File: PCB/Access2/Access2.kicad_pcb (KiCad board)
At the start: 2 copper layers, 50 x 26.5 mm, 67 parts, among them J1 USB-C, J2 RFID, J3 INPUTS, J4 Shelly, J5 POWER, J6 DOOR, Q1 NX7002AK, SW1 ESE13V01D, U1 ESP32-PICO-MINI-02, U2 FT231XQ, U3 G3VM-41GR8, U4 LMR16006XDDCR, U5 LMR16006XDDCR, U6 AA, U7 QR

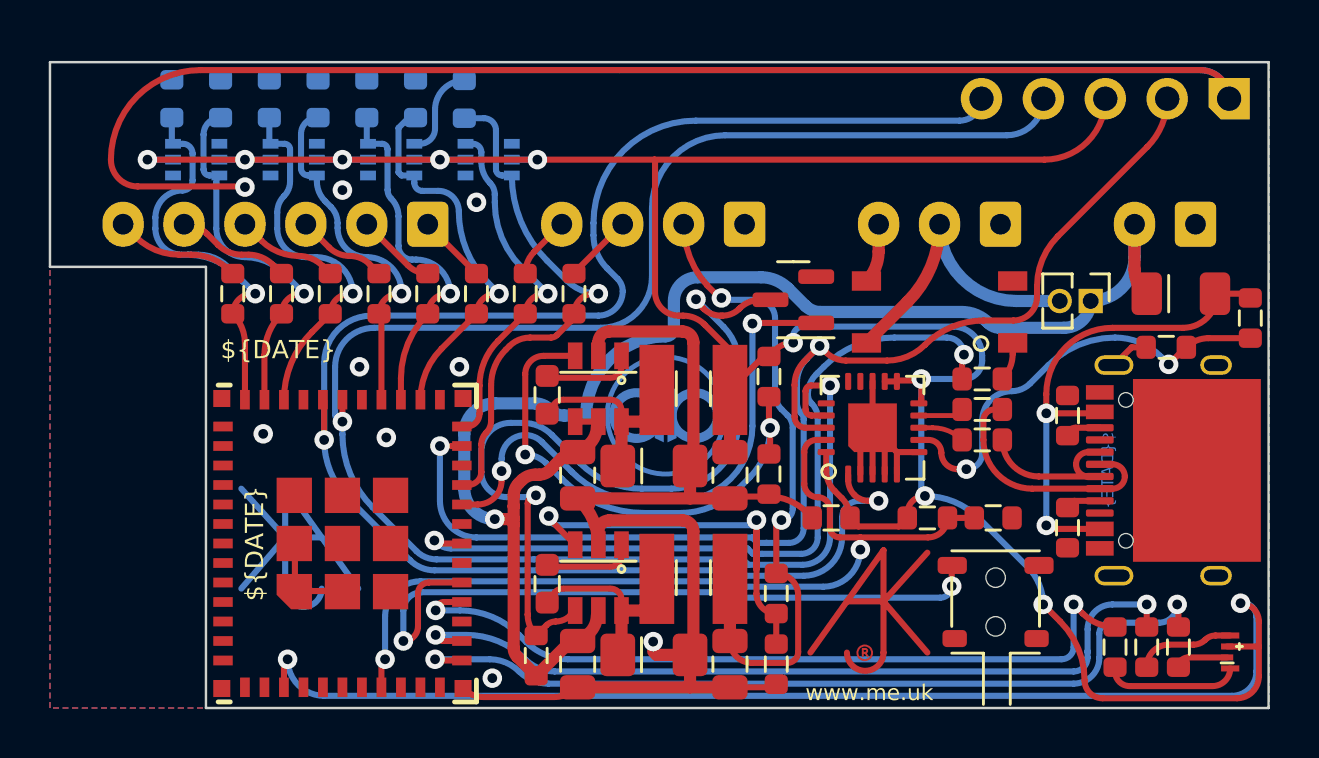
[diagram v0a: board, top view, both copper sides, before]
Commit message: Reverse polarity protection and additional capacitors for less clean supplies.
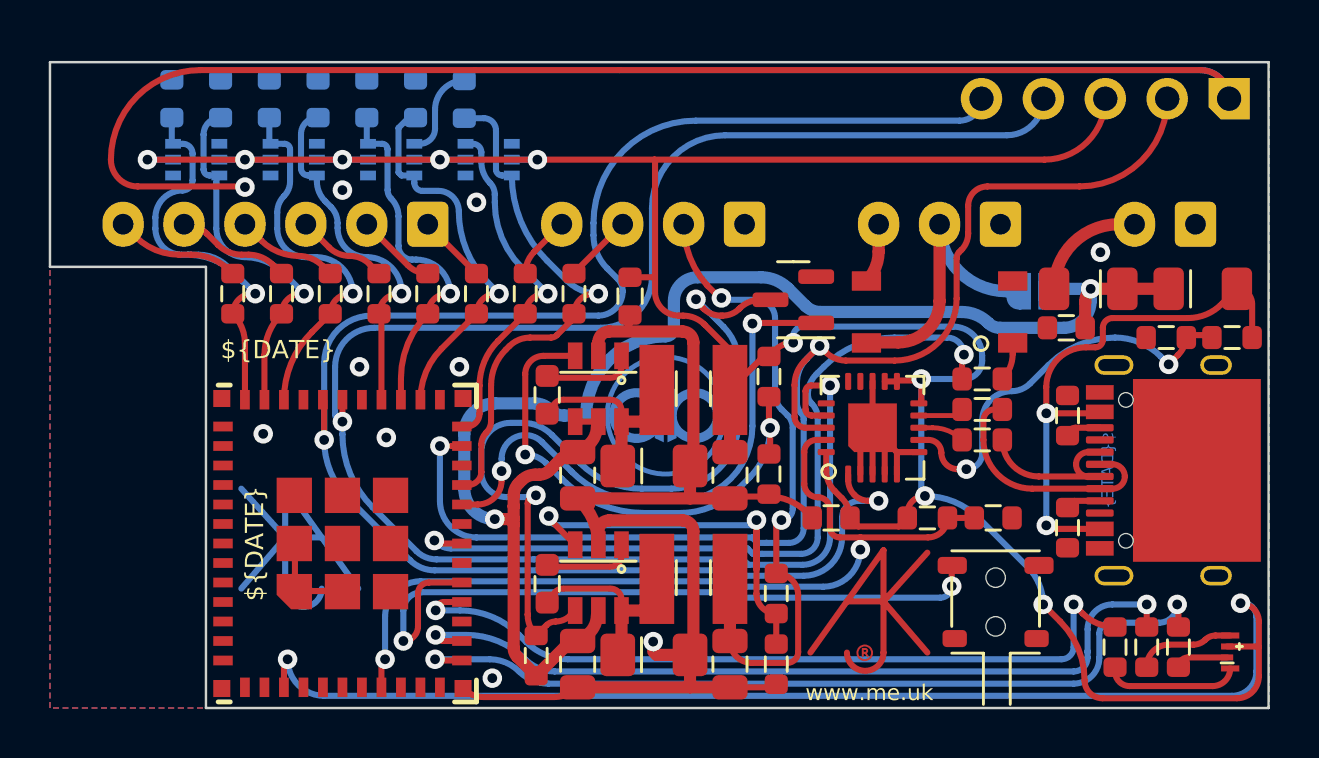
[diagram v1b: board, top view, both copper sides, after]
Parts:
- added C16: 10nF, RevK:C_0603, F.Cu at (123.8, 75.6)
- added C17: 10uF, RevK:C_0603, F.Cu at (141.7, 76.9)
- added D9: D, RevK:D_1206, F.Cu at (142.6, 75.3)
- JP1: footprint Connector_PinHeader_1.27mm:PinHeader_1x02_P1.27mm_Vertical -> Jumper:SolderJumper-2_P1.3mm_Open_RoundedPad1.0x1.5mm; moved to B.Cu
- moved JP1 2.33 mm to (140.4, 75.4), turned to 180 degrees
- moved R2 1.10 mm to (148.5, 77.3), turned to 180 degrees
- moved D8 0.92 mm to (147.3, 75.3)
- moved R3 0.40 mm to (145.8, 77.3)
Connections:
- J5 pad 2: +12V -> DC
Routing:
- net DC: track 0.00 -> 4.71 mm
- net VBUS: track 20.7 -> 22.4 mm
- net BOOT: track 52.1 -> 53.6 mm
- net Net-(R2-Pad2): track 17.9 -> 16.7 mm
- net GND: track 120.4 -> 119.3 mm, vias 9 -> 10
- net +3V3: track 158.8 -> 159.8 mm
- net Net-(J6-Pad2): track 12.5 -> 11.8 mm
- net +12V: vias 1 -> 2

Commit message: Position
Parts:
- C17: footprint RevK:C_0603 -> RevK:C_0805
- moved C17 0.28 mm to (141.9, 77.1)
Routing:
- net GND: track 119.3 -> 122.2 mm
- net +12V: track 57.6 -> 59.4 mm
- net VBUS: track 22.4 -> 23.3 mm, vias 2 -> 3

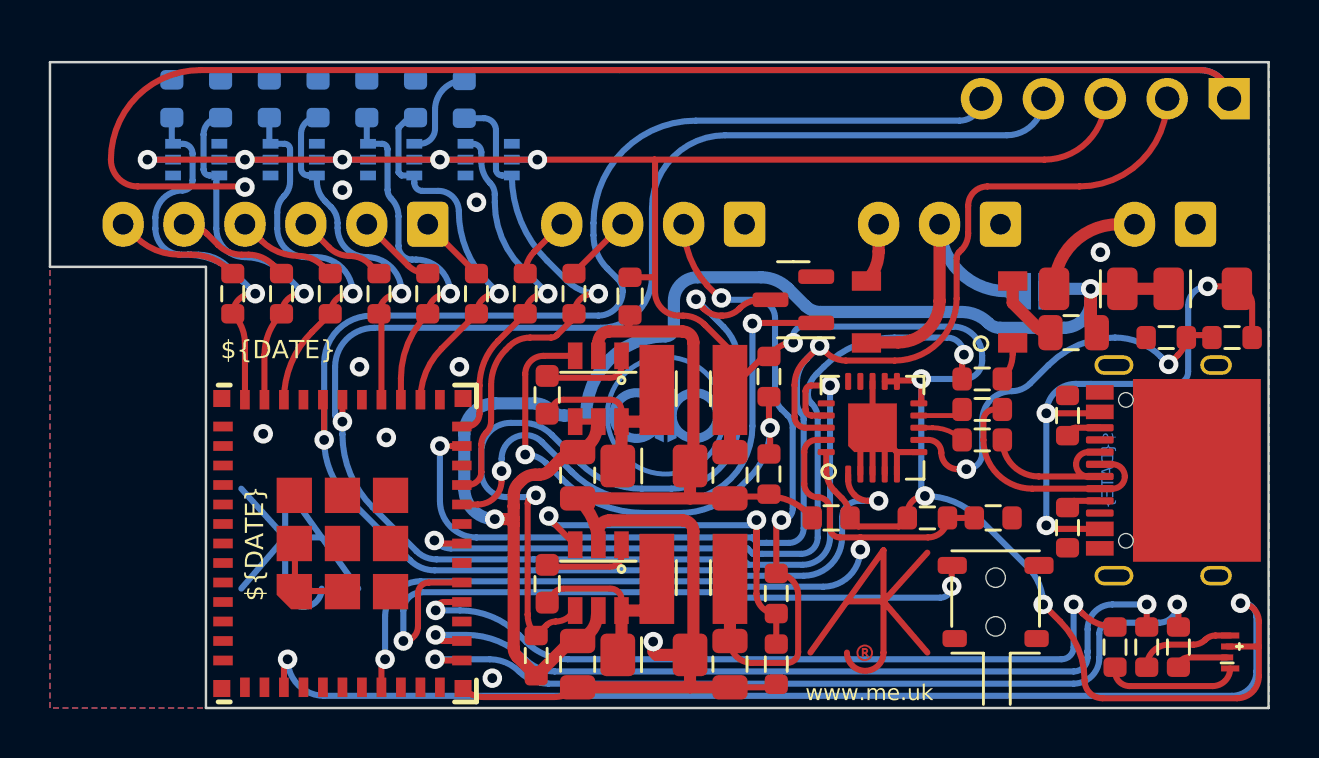
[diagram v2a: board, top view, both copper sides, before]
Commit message: Added FET on NFC Rx
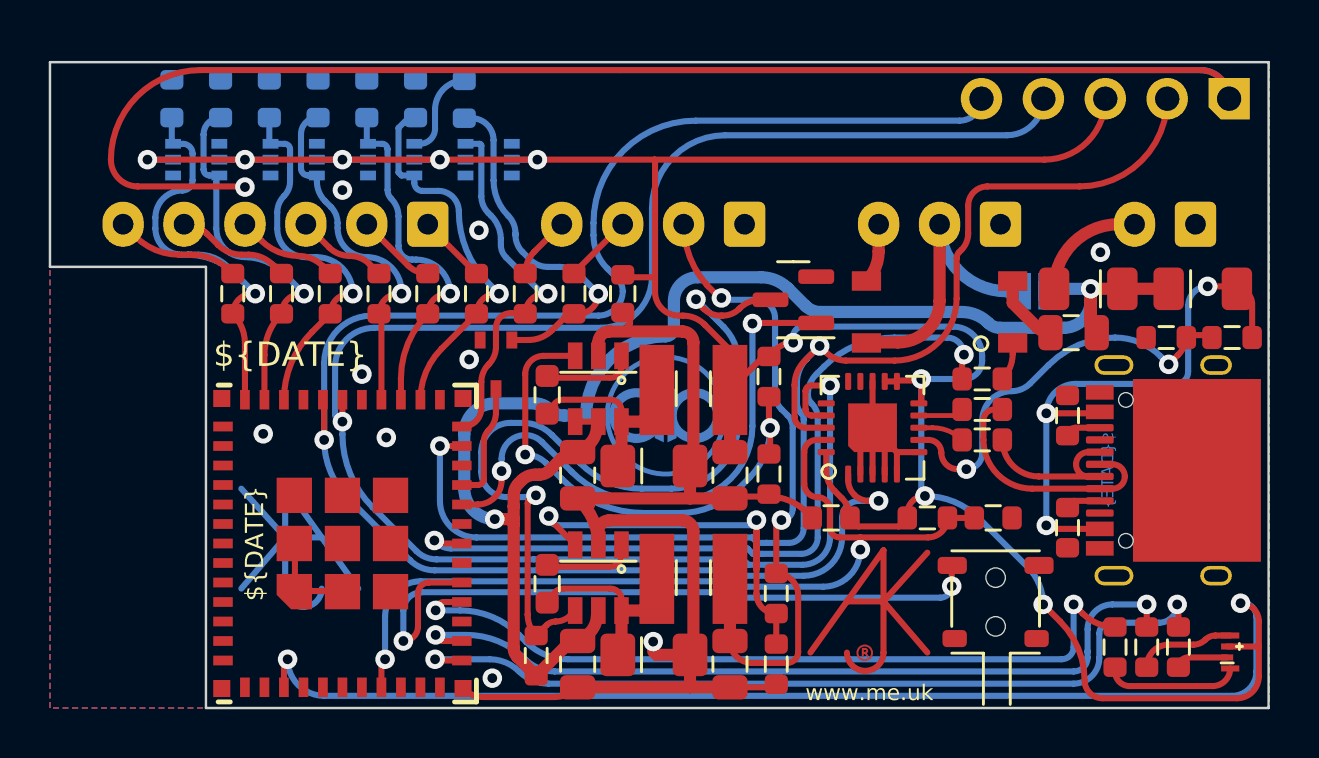
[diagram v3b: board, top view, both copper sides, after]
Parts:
- added Q2: PMF250XNEX, RevK:SOT-323_SC-70, F.Cu at (118.3, 78.4)
- moved C16 0.32 mm to (123.5, 75.5)
- turned C2 to -90 degrees
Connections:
- net IN1 renamed IO1
- net IN2 renamed IO2
- net IN3 renamed IO3
- net IN4 renamed IO4
- net IN5 renamed IO5
- net IN6 renamed IO6
- C1 pad 1: +3V3 -> +3.3V
- C16 pad 1: +3V3 -> +3.3V
- C2 pad 1: RFRX -> GND
- C2 pad 2: GND -> Net-(C2-Pad2)
- D1 pad 1: GND -> (no net)
- D1 pad 2: +3V3 -> (no net)
- D1 pad 5: +3V3 -> +3.3V
- D1 pad 6: RFRX -> (no net)
- D2 pad 2: +3V3 -> +3.3V
- D2 pad 5: +3V3 -> +3.3V
- D3 pad 2: +3V3 -> +3.3V
- D3 pad 5: +3V3 -> +3.3V
- D4 pad 2: +3V3 -> +3.3V
- D4 pad 5: +3V3 -> +3.3V
- D5 pad 2: +3V3 -> +3.3V
- J4 pad 3: +3V3 -> +3.3V
- R1 pad 1: +3V3 -> +3.3V
- R22 pad 1: +3V3 -> +3.3V
- R6 pad 2: RFRX -> Net-(C2-Pad2)
- U1 pad 3: +3V3 -> +3.3V
- U2 pad 10: +3V3 -> +3.3V
- U2 pad 11: +3V3 -> +3.3V
- U2 pad 12: +3V3 -> +3.3V
- U2 pad 20: +3V3 -> +3.3V
- U5 pad 7: +3V3 -> +3.3V
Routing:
- net +3V3: track 159.8 -> 0.00 mm, vias 11 -> 0
- net +3.3V: track 0.00 -> 158.8 mm, vias 0 -> 11
- net RFRX: track 21.6 -> 4.86 mm, vias 1 -> 0
- net Net-(C2-Pad2): track 0.00 -> 14.6 mm, vias 0 -> 1
- net RFTX: track 14.6 -> 15.4 mm

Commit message: New connectors
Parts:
- J2: footprint RevK:Molex_MiniSPOX_H4RA -> RevK:PTSM-HH-4-RA
- J3: footprint RevK:Molex_MiniSPOX_H6RA -> RevK:PTSM-HH-6-RA
- J4: moved to F.Cu
- J5: footprint RevK:Molex_MiniSPOX_H2RA -> RevK:PTSM-HH1-2-RA
- J6: footprint RevK:Molex_MiniSPOX_H3RA -> RevK:PTSM-HH1-3-RA
- moved J4 18.6 mm to (124.7, 67.9)
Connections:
- net OUT1 renamed RELAY
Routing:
- net GND: track 122.2 -> 66.3 mm
- net +3.3V: track 158.8 -> 138.3 mm
- net I: track 72.7 -> 59.2 mm
- net O: track 70.0 -> 56.9 mm
- net IO6: track 18.8 -> 16.3 mm
- net BOOT: track 53.6 -> 55.6 mm
- net +12V: track 59.4 -> 58.7 mm
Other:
- board size 50 x 26.5 mm -> 50 x 27 mm
- board text added: "DC"
